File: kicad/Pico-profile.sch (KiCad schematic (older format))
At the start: 32 parts, among them J1 Parallel, J2 DB25_Female, J3 Micro_SD_Card, J4 I2C, U1 74LS280, U2 74LS244, U3 74LVC244, U4 74LVC2G240, U5 74LVC1G04, U6 74LVC244, U7 Pico, U8 74LVC1G07

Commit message: Intermediate commit. Worked on hardware
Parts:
- removed U6: 74LVC244, Package_SO:TSSOP-20_4.4x6.5mm_P0.65mm, symbol 74xx:74LS244
- added R1: 0, Resistor_SMD:R_0603_1608Metric, symbol Device:R
- added R14, R15, R16, R17, R18: 100, Resistor_SMD:R_0603_1608Metric, symbol Device:R
- added U6, U9: 74LVC1G04, Package_TO_SOT_SMD:SOT-23-5_HandSoldering, symbol pico-profile-lib:74LVC1G04
- J3: footprint Connector_Card:microSD_HC_Hirose_DM3AT-SF-PEJM5 -> Connector_Card:microSD_HC_Molex_104031-0811
- U2, U3: footprint Package_SO:SOP-20_7.5x12.8mm_P1.27mm -> Package_SO:SOIC-20W_7.5x12.8mm_P1.27mm
- renumbered R9 to R10, R10 to R11, R11 to R12, R12 to R13, R1 to R2, R2 to R3, R3 to R4, R4 to R5, R5 to R6, R6 to R7, R7 to R8, R8 to R9
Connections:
- net +3V3: now also U6.5 (VCC), U9.5 (VCC)
- net GND: now also R1.1, U6.3 (GND), U9.3 (GND); no longer J1.25 (Pin_25), J2.25 (P25)
- net ID0: now also U3.9 (O0b); no longer U3.18 (O0a)
- net ID1: now also U3.12 (O3a); no longer U3.16 (O1a)
- net ID3: now also U3.16 (O1a); no longer U3.12 (O3a)
- net ID4: now also U3.18 (O0a); no longer U3.9 (O0b)
- net OD0: now also U2.11 (I0b); no longer U2.2 (I0a)
- net OD1: now also U2.8 (I3a); no longer U2.4 (I1a)
- net OD3: now also U2.4 (I1a); no longer U2.8 (I3a)
- net OD4: now also U2.2 (I0a); no longer U2.11 (I0b)
- net PD0: now also U2.9 (O0b), U3.11 (I0b); no longer U2.18 (O0a), U3.2 (I0a)
- net PD1: now also U2.12 (O3a), U3.8 (I3a); no longer U2.16 (O1a), U3.4 (I1a)
- net PD3: now also U2.16 (O1a), U3.4 (I1a); no longer U2.12 (O3a), U3.8 (I3a)
- net PD4: now also U2.18 (O0a), U3.2 (I0a); no longer U2.9 (O0b), U3.11 (I0b)
- net PR~W: now also R16.1; no longer U5.2
- net ~PBSY: now also R15.2; no longer U4.3
- net ~PCMD: now also R17.2
- net ~PPARITY: now also R14.1
- net ~PRES: now also U8.2
- net ~PSTRB: now also R18.2
- net ~CMD renamed CMD
- net CMD: now also U6.4
- net ~STRB renamed STRB
- net STRB: now also U9.4
- net ~TPARITY: no longer names the net of U4.6
- net ~TPARITY: now also R14.2
- new net: R15.1, U4.3
- new net: R16.2, U5.2
- new net: R17.1, U6.2
- new net: R18.1, U9.2
- new net PCHK: J1.25 (Pin_25), J2.25 (P25), R1.2
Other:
- moved on the sheet: U8

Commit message: Hardware first revision. Need cosmetic changes
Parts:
- added D1: MBR1020VL, Diode_SMD:D_SOD-123F, symbol Diode:MBR1020VL
- added J5: Screw_Terminal_01x02, Connector_Phoenix_MSTB:PhoenixContact_MSTBA_2,5_2-G-5,08_1x02_P5.08mm_Horizontal, symbol Connector:Screw_Terminal_01x02
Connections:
- net +3V3: now also C2.1
- net +5VL: now also D1.1 (K); no longer C2.1
- net GND: now also J5.1 (Pin_1)
- new net: D1.2 (A), J5.2 (Pin_2)
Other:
- moved on the sheet: C2, C3
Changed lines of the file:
@@
 L Device:C C3
 U 1 1 60ED2254
-P 8450 1000
-F 0 "C3" H 8565 1046 50  0000 L CNN
-F 1 "10uF" H 8550 900 50  0000 L CNN
-F 2 "Capacitor_SMD:C_0603_1608Metric" H 8488 850 50  0001 C CNN
-F 3 "~" H 8450 1000 50  0001 C CNN
-	1    8450 1000
+P 8000 1000
+F 0 "C3" H 8115 1046 50  0000 L CNN
+F 1 "10uF" H 8100 900 50  0000 L CNN
+F 2 "Capacitor_SMD:C_0603_1608Metric" H 8038 850 50  0001 C CNN
+F 3 "~" H 8000 1000 50  0001 C CNN
+	1    8000 1000
 	1    0    0    -1
 $EndComp
@@
 	9450 800  9450 750
 Wire Wire Line
-	8450 1150 8450 1250
-Wire Wire Line
-	8450 1250 8950 1250
+	8000 1150 8000 1250
+Wire Wire Line
+	8000 1250 8550 1250
 Connection ~ 8950 1250
 Wire Wire Line
@@
 L Device:C C2
 U 1 1 61BB4F16
-P 8000 1000
-F 0 "C2" H 8115 1046 50  0000 L CNN
-F 1 "100nF" H 8100 900 50  0000 L CNN
-F 2 "Capacitor_SMD:C_0603_1608Metric" H 8038 850 50  0001 C CNN
-F 3 "~" H 8000 1000 50  0001 C CNN
-	1    8000 1000
+P 8550 1000
+F 0 "C2" H 8665 1046 50  0000 L CNN
+F 1 "100nF" H 8650 900 50  0000 L CNN
+F 2 "Capacitor_SMD:C_0603_1608Metric" H 8588 850 50  0001 C CNN
+F 3 "~" H 8550 1000 50  0001 C CNN
+	1    8550 1000
 	1    0    0    -1
 $EndComp
@@
 Wire Wire Line
 	7600 1150 7600 1250
-Wire Wire Line
-	7600 1250 8000 1250
-Connection ~ 8450 1250
-Wire Wire Line
-	8000 1150 8000 1250
 Connection ~ 8000 1250
 Wire Wire Line
-	8000 1250 8450 1250
-Wire Wire Line
 	7600 850  7600 800
 Wire Wire Line
 	7600 800  8000 800
-Wire Wire Line
-	8000 850  8000 800
-Connection ~ 8000 800
-Wire Wire Line
-	8000 800  8450 800
 Wire Wire Line
 	8950 850  8950 800
@@
 	2750 6550 3450 6550
 Wire Wire Line
-	8450 800  8450 850
+	8000 800  8000 850
 $Comp
 L power:+3V3 #PWR017
@@
 Wire Wire Line
 	2550 5100 2650 5100
+Wire Wire Line
+	7600 1250 8000 1250
+Connection ~ 8000 800
+Wire Wire Line
+	8550 1150 8550 1250
+Connection ~ 8550 1250
+Wire Wire Line
+	8550 1250 8950 1250
+Wire Wire Line
+	8950 800  8550 800
+Wire Wire Line
+	8550 800  8550 850
+Connection ~ 8950 800
+$Comp
+L Connector:Screw_Terminal_01x02 J5
+U 1 1 61277E40
+P 7050 1050
+F 0 "J5" H 6968 1267 50  0000 C CNN
+F 1 "Screw_Terminal_01x02" H 6968 1176 50  0000 C CNN
+F 2 "Connector_Phoenix_MSTB:PhoenixContact_MSTBA_2,5_2-G-5,08_1x02_P5.08mm_Horizontal" H 7050 1050 50  0001 C CNN
+F 3 "~" H 7050 1050 50  0001 C CNN
+	1    7050 1050
+	-1   0    0    1
+$EndComp
+Wire Wire Line
+	7250 950  7250 800
+Wire Wire Line
+	7250 1050 7250 1250
+Wire Wire Line
+	7250 1250 7600 1250
+Connection ~ 7600 1250
+$Comp
+L Diode:MBR1020VL D1
+U 1 1 614028B7
+P 7400 800
+F 0 "D1" H 7400 584 50  0000 C CNN
+F 1 "MBR1020VL" H 7400 675 50  0000 C CNN
+F 2 "Diode_SMD:D_SOD-123F" H 7400 625 50  0001 C CNN
+F 3 "https://www.onsemi.com/pub/Collateral/MBR1020VL-D.PDF" H 7400 800 50  0001 C CNN
+	1    7400 800
+	-1   0    0    1
+$EndComp
+Wire Wire Line
+	7550 800  7600 800
 Wire Bus Line
 	3450 1350 3450 2350

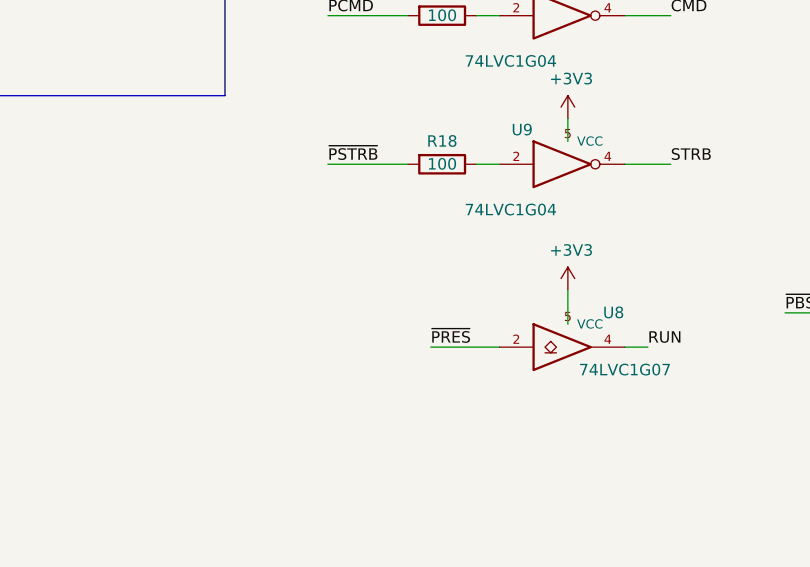
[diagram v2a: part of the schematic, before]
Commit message: Cosmetic changes on PCB
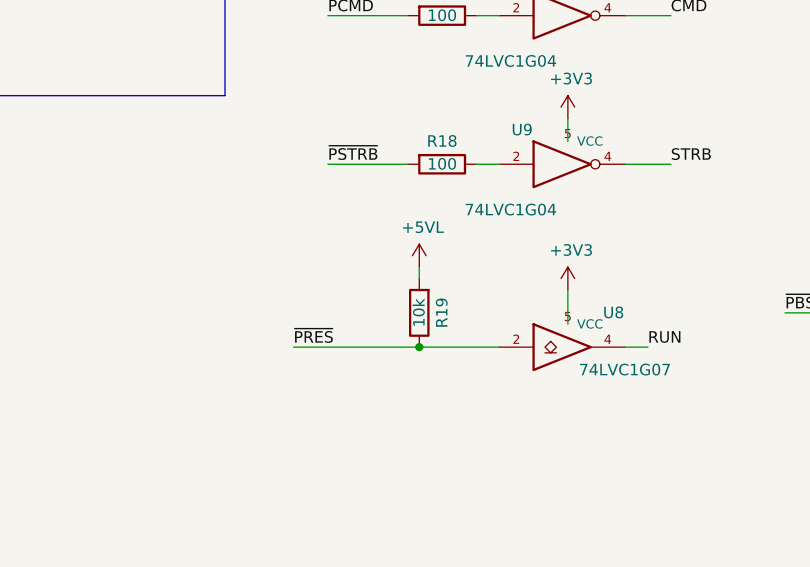
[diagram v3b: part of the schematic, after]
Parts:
- added R19: 10k, Resistor_SMD:R_0603_1608Metric, symbol Device:R
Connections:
- net +5VL: now also R19.2
- net ~PRES: now also R19.1
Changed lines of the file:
@@
 Text Label 9050 6250 0    50   ~ 0
 RUN
-Text Label 8100 6250 0    50   ~ 0
+Text Label 7500 6250 0    50   ~ 0
 ~PRES
 Text Label 9150 4800 0    50   ~ 0
@@
 	9650 6100 9950 6100
 Wire Wire Line
-	8100 6250 8400 6250
+	7500 6250 8050 6250
 $Comp
 L pico-profile-lib:74LVC1G04 U6
@@
 Wire Wire Line
 	7550 800  7600 800
+$Comp
+L Device:R R19
+U 1 1 6129DB38
+P 8050 6100
+F 0 "R19" V 7950 6100 50  0000 C CNN
+F 1 "10k" V 8050 6100 50  0000 C CNN
+F 2 "Resistor_SMD:R_0603_1608Metric" V 7980 6100 50  0001 C CNN
+F 3 "~" H 8050 6100 50  0001 C CNN
+	1    8050 6100
+	-1   0    0    1
+$EndComp
+Connection ~ 8050 6250
+Wire Wire Line
+	8050 6250 8400 6250
+$Comp
+L power:+5VL #PWR0103
+U 1 1 612B3D43
+P 8050 5900
+F 0 "#PWR0103" H 8050 5750 50  0001 C CNN
+F 1 "+5VL" H 8065 6073 50  0000 C CNN
+F 2 "" H 8050 5900 50  0001 C CNN
+F 3 "" H 8050 5900 50  0001 C CNN
+	1    8050 5900
+	1    0    0    -1
+$EndComp
+Wire Wire Line
+	8050 5950 8050 5900
 Wire Bus Line
 	3450 1350 3450 2350

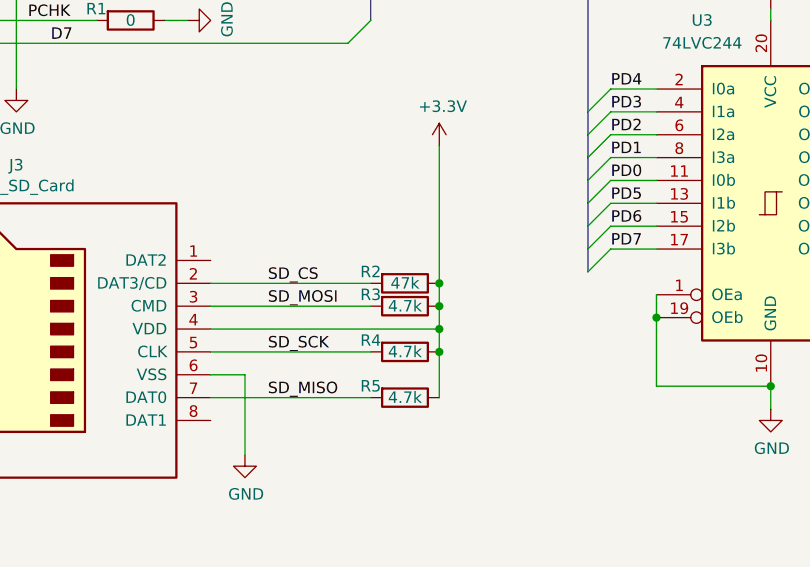
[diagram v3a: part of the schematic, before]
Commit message: Started implementing the tester
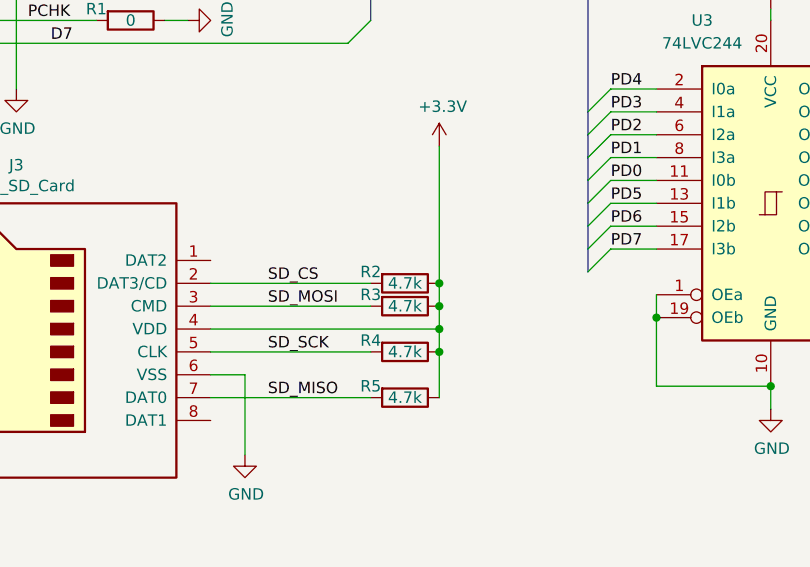
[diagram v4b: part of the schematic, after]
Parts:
- R2: value 47k -> 4.7k
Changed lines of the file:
@@
 P 3600 6250
 F 0 "R2" V 3550 6100 50  0000 C CNN
-F 1 "47k" V 3600 6250 50  0000 C CNN
+F 1 "4.7k" V 3600 6250 50  0000 C CNN
 F 2 "Resistor_SMD:R_0603_1608Metric" V 3530 6250 50  0001 C CNN
 F 3 "~" H 3600 6250 50  0001 C CNN

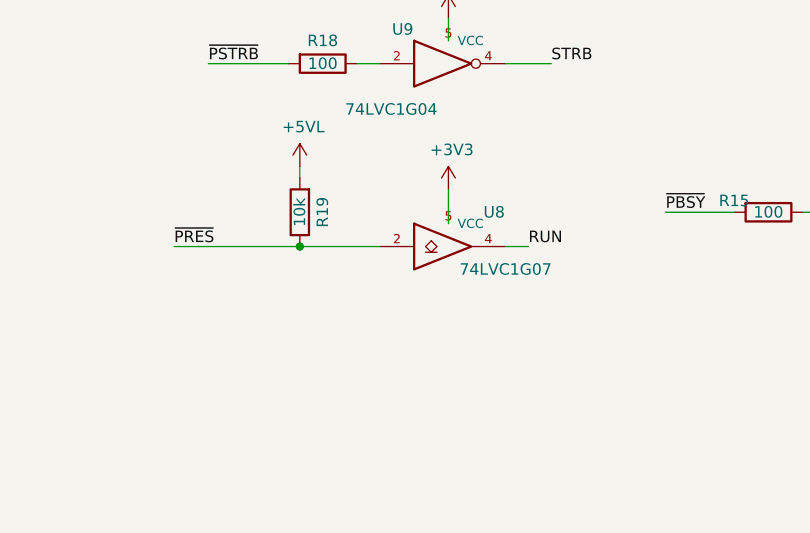
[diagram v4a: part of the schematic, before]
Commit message: Fixed PCB footprint. Added more silkscreen information.
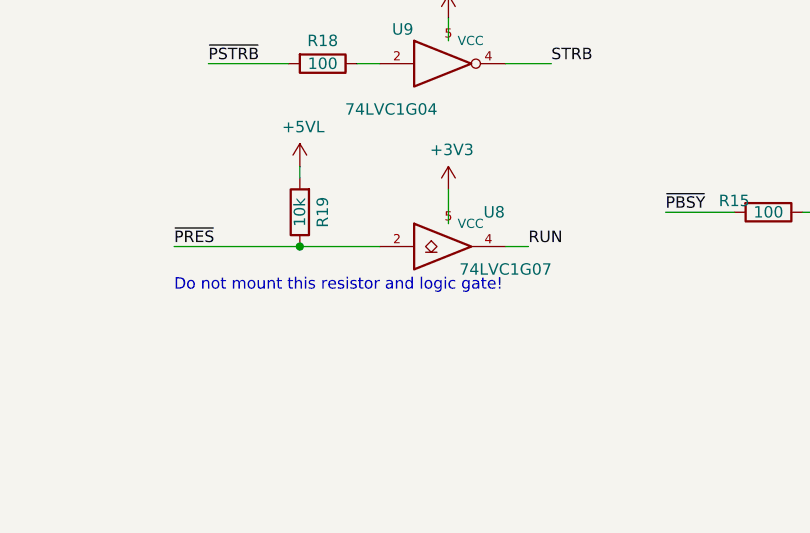
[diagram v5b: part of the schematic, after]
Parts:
- U1: footprint Package_SO:SO-14_3.9x8.65mm_P1.27mm -> Package_SO:SO-16_5.3x10.2mm_P1.27mm
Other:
- note added: "Do not mount this resistor and logic gate!"
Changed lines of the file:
@@
 F 0 "U1" H 4900 2300 50  0000 C CNN
 F 1 "74LS280" H 4900 2200 50  0000 C CNN
-F 2 "Package_SO:SO-14_3.9x8.65mm_P1.27mm" H 5150 1600 50  0001 C CNN
+F 2 "Package_SO:SO-16_5.3x10.2mm_P1.27mm" H 5150 1600 50  0001 C CNN
 F 3 "http://www.ti.com/lit/gpn/sn74LS280" H 5150 1600 50  0001 C CNN
 	1    5150 1600
@@
 Wire Bus Line
 	4400 1050 4400 6200
+Text Notes 7500 6450 0    50   ~ 0
+Do not mount this resistor and logic gate!
 $EndSCHEMATC
